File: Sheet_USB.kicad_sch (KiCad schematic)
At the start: 12 parts, among them J4 USB_A, U12 USB3300-EZK, U17 MIC2005A-1YM5, U18 TPD1E05U06DYA, X1 ECS-2333-240-BN

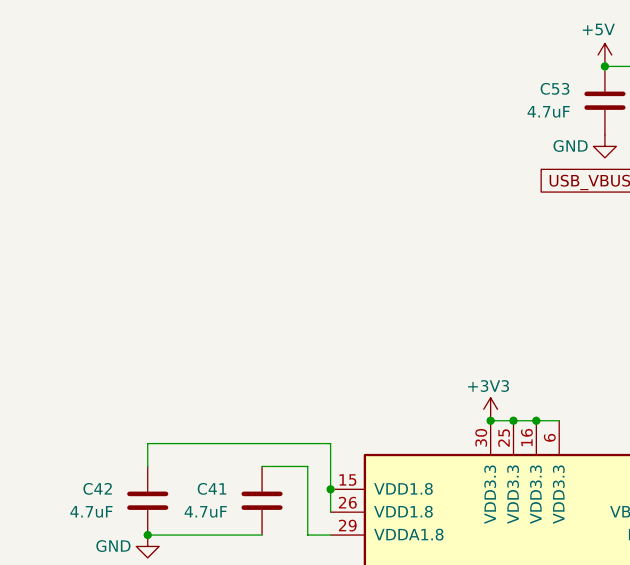
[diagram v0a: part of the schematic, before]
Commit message: added some capacitors to various components that weren't capacitored enough
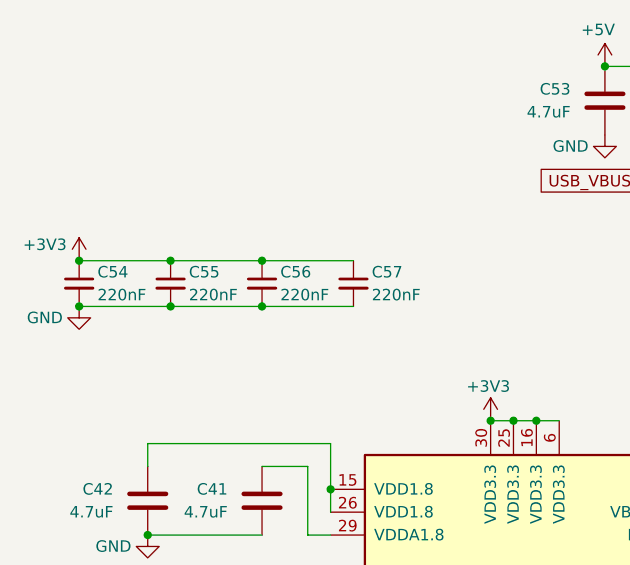
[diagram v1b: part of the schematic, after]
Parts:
- added C54, C55, C56, C57: 220nF, Capacitor_SMD:C_0201_0603Metric_Pad0.64x0.40mm_HandSolder, symbol Device:C_Small
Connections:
- net +3V3: now also C54.1, C55.1, C56.1, C57.1
- net GND: now also C54.2, C55.2, C56.2, C57.2
